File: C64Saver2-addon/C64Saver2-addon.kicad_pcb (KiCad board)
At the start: 2 copper layers, 45.7 x 35.6 mm, 12 parts, among them J1 Conn_01x12_Female, J2 Conn_01x07_Female, J3 Conn_01x04_Male, SW1 SW_Push, SW2 SW_Push, U1 ProMicro, U3 INA219, U5 4N25, U6 ADuM1200BR, U7 4N25

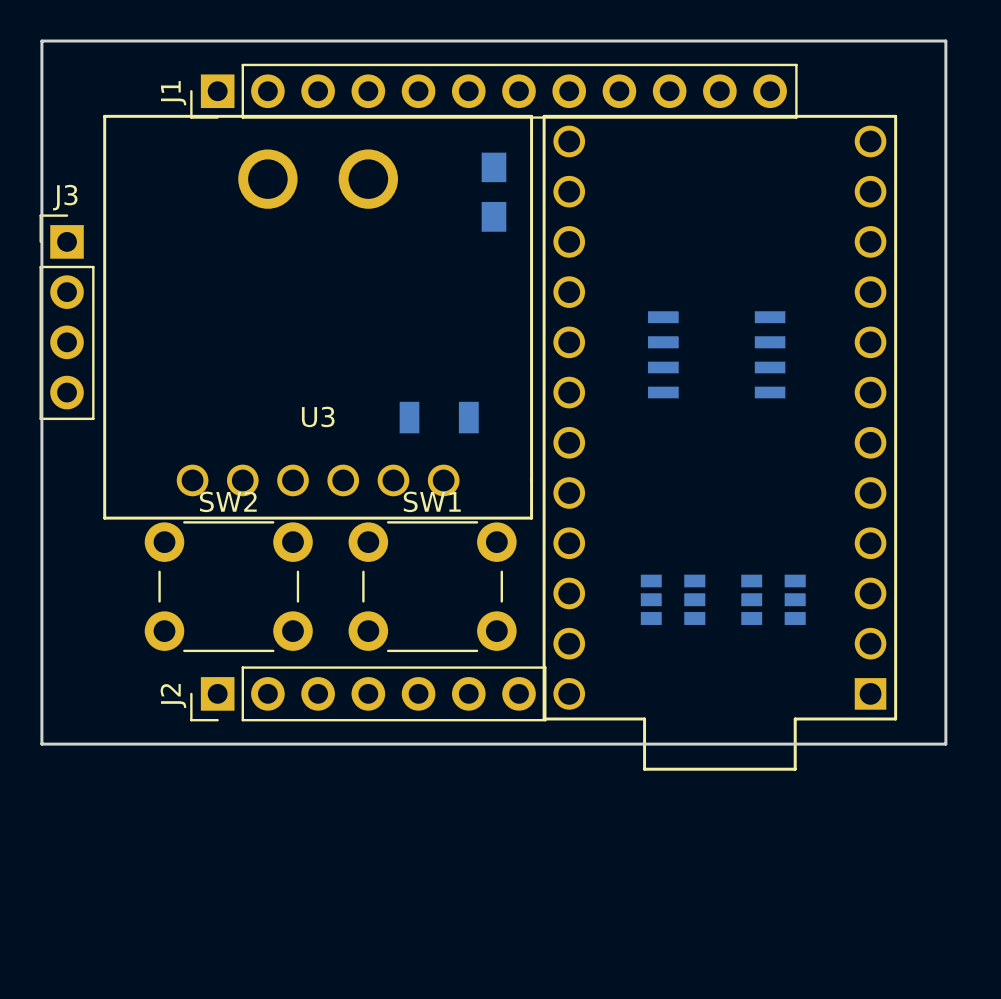
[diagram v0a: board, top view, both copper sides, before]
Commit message: Tidy up project libraries. Relative paths
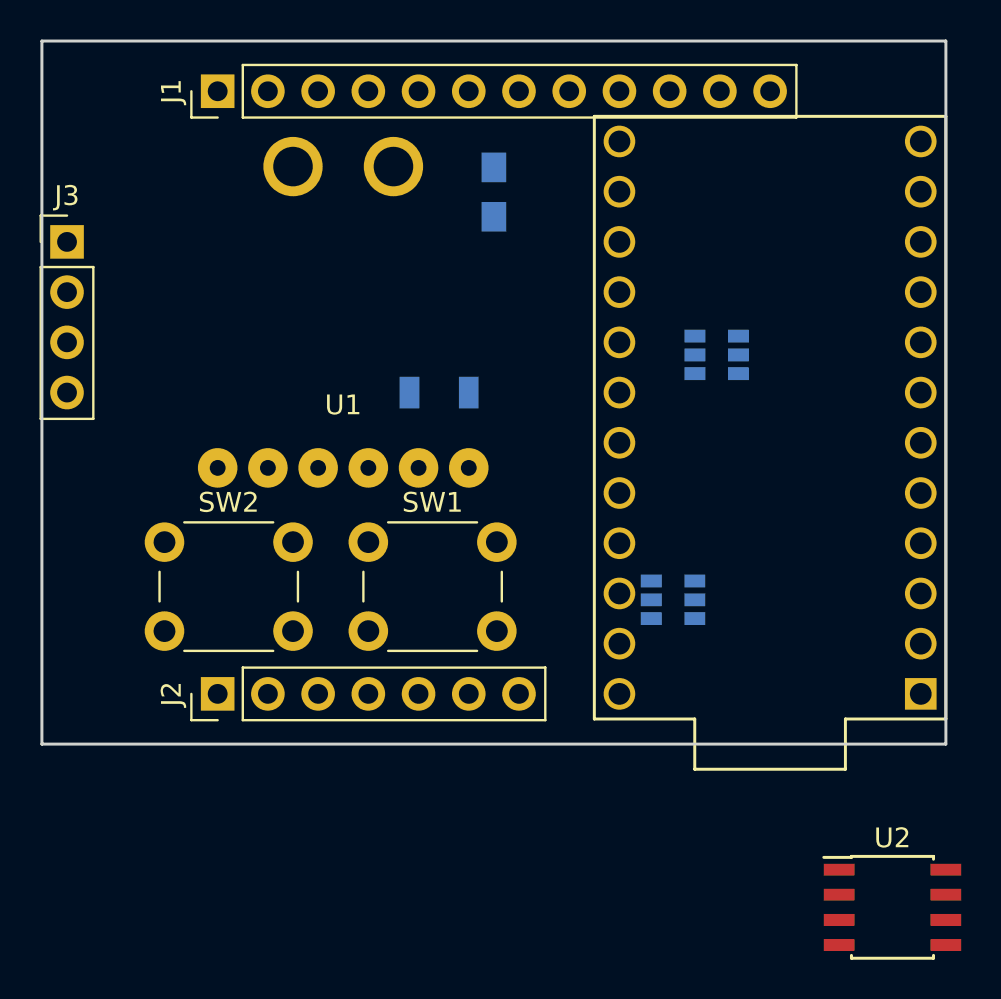
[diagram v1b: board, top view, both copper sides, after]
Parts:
- removed U7: 4N25, TO_SOT_Packages_SMD:SOT-23-6
- added U2: ADuM1200BR, Housings_SOIC:SOIC-8_3.9x4.9mm_Pitch1.27mm, F.Cu at (181.4, 125.1)
- U1: value ProMicro -> INA219; footprint promicro:ProMicro -> ina219:ina219
- U3: value INA219 -> ProMicro; footprint ina216:ina216board -> promicro:ProMicro
- U6: value ADuM1200BR -> 4N25; footprint Housings_SOIC:SOIC-8_3.9x4.9mm_Pitch1.27mm -> TO_SOT_Packages_SMD:SOT-23-6
- moved U3 23.1 mm to (175.3, 100.3), turned to 90 degrees
- moved U1 19.2 mm to (153.7, 102.9), turned to 0 degrees
- moved D1 1.27 mm to (158.5, 99.1)
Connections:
- U1 pad 3: GND -> Net-(U1-Pad3)
- U1 pad 4: GND -> Net-(U1-Pad4)
- U1 pad 5: Net-(J3-Pad4) -> (no net)
- U1 pad 6: Net-(J3-Pad3) -> (no net)
- U1 pad 7: Net-(SW2-Pad2) -> VIN-
- U3 pad 3: Net-(U3-Pad3) -> GND
- U3 pad 4: Net-(U3-Pad4) -> GND
- U3 pad 5: (no net) -> Net-(J3-Pad4)
- U3 pad 6: (no net) -> Net-(J3-Pad3)
- U3 pad 7: VIN- -> Net-(SW1-Pad2)
- U3 pad 8: /VIN+ -> Net-(SW2-Pad2)
- U6 pad 1: VIN- -> (no net)
- U6 pad 2: Net-(U3-Pad4) -> GND
- U6 pad 3: Net-(U3-Pad3) -> (no net)
- U6 pad 4: GND2 -> PGATE
- U6 pad 5: GND -> VIN-
- U6 pad 6: Net-(J3-Pad3) -> (no net)
